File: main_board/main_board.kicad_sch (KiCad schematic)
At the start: 56 parts, among them J1 USB4105-GF-A-060, J2 Conn_ARM_JTAG_SWD_10, Q3 NX3008PBK,215, U1 SSD1306, U2 ESP32-S2-SOLO, U3 TLV62568PDRLT, U4 MCP73832, U5 DW01, U6 8205A, U7 MAX17055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

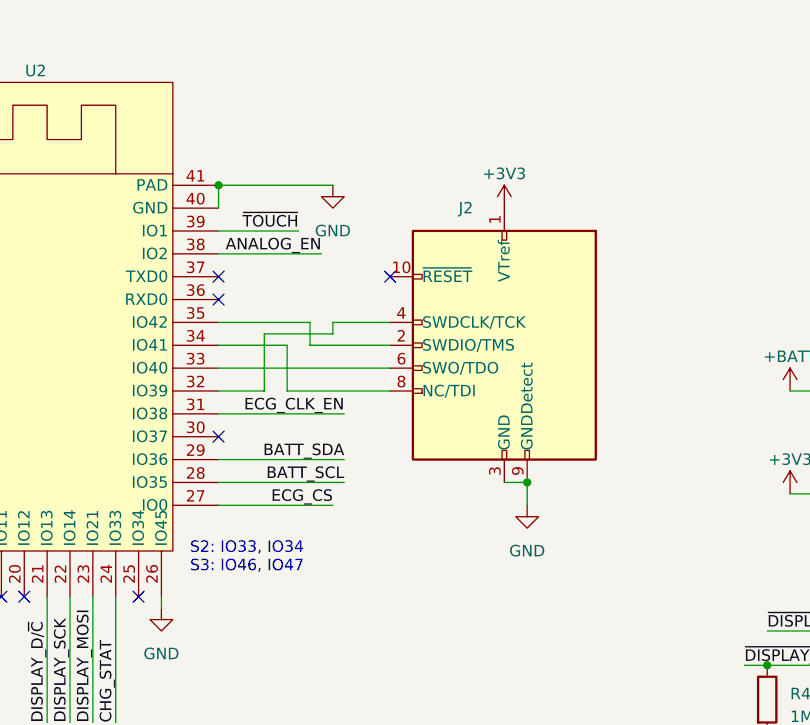
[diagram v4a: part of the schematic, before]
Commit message: Remove JTAG port
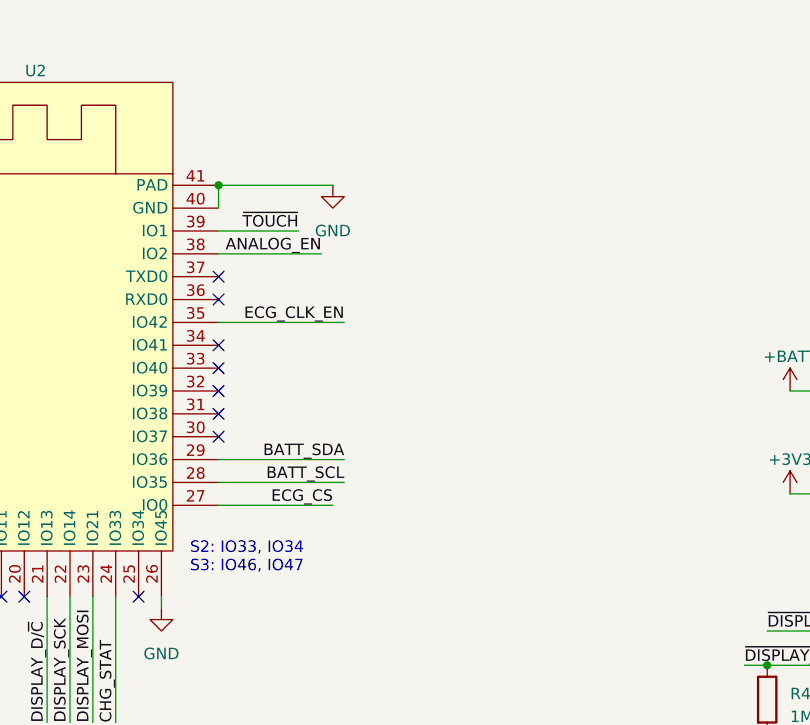
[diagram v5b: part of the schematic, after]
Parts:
- removed J2: Conn_ARM_JTAG_SWD_10, Connector:Tag-Connect_TC2050-IDC-NL_2x05_P1.27mm_Vertical, symbol Connector:Conn_ARM_JTAG_SWD_10
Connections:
- net ECG_CLK_EN: now also U2.35 (IO42); no longer U2.31 (IO38)
- no-connect marks 16 -> 19
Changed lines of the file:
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@@
   (junction (at 200.66 130.81) (diameter 0) (color 0 0 0 0)
   )
-  (junction (at 204.47 66.04) (diameter 0) (color 0 0 0 0)
-  )
   (junction (at 71.12 139.7) (diameter 0) (color 0 0 0 0)
   )
@@
   (junction (at 102.87 55.88) (diameter 0) (color 0 0 0 0)
   )
+  (no_connect (at 170.18 55.88))
+  (no_connect (at 170.18 53.34))
   (no_connect (at 254 109.22))
   (no_connect (at 138.43 78.74))
   (no_connect (at 170.18 60.96))
+  (no_connect (at 170.18 58.42))
   (no_connect (at 170.18 45.72))
-  (no_connect (at 189.23 43.18))
   (no_connect (at 198.12 144.78))
   (no_connect (at 148.59 78.74))
@@
   (no_connect (at 198.12 147.32))
   (no_connect (at 81.28 162.56))
+  (no_connect (at 170.18 50.8))
   (wire (pts (xy 116.84 58.42) (xy 129.54 58.42))
     (stroke (width 0) (type default))
@@
     (stroke (width 0) (type default))
   )
-  (wire (pts (xy 180.34 48.26) (xy 180.34 50.8))
-    (stroke (width 0) (type default))
-  )
   (wire (pts (xy 121.92 35.56) (xy 129.54 35.56))
     (stroke (width 0) (type default))
@@
     (stroke (width 0) (type default))
   )
-  (wire (pts (xy 177.8 50.8) (xy 177.8 55.88))
-    (stroke (width 0) (type default))
-  )
   (wire (pts (xy 158.75 177.8) (xy 158.75 186.69))
     (stroke (width 0) (type default))
@@
     (stroke (width 0) (type default))
   )
-  (wire (pts (xy 182.88 48.26) (xy 189.23 48.26))
-    (stroke (width 0) (type default))
-  )
   (wire (pts (xy 198.12 121.92) (xy 201.93 121.92))
     (stroke (width 0) (type default))
@@
     (stroke (width 0) (type default))
   )
-  (wire (pts (xy 182.88 49.53) (xy 182.88 48.26))
-    (stroke (width 0) (type default))
-  )
   (wire (pts (xy 129.54 175.26) (xy 129.54 177.8))
     (stroke (width 0) (type default))
@@
     (stroke (width 0) (type default))
   )
-  (wire (pts (xy 180.34 50.8) (xy 189.23 50.8))
-    (stroke (width 0) (type default))
-  )
   (wire (pts (xy 33.02 130.81) (xy 33.02 134.62))
     (stroke (width 0) (type default))
@@
     (stroke (width 0) (type default))
   )
-  (wire (pts (xy 175.26 55.88) (xy 175.26 49.53))
-    (stroke (width 0) (type default))
-  )
   (wire (pts (xy 80.01 134.62) (xy 82.55 134.62))
     (stroke (width 0) (type default))
   )
-  (wire (pts (xy 170.18 50.8) (xy 177.8 50.8))
-    (stroke (width 0) (type default))
-  )
   (wire (pts (xy 26.67 151.13) (xy 26.67 165.1))
     (stroke (width 0) (type default))
@@
     (stroke (width 0) (type default))
   )
-  (wire (pts (xy 170.18 48.26) (xy 180.34 48.26))
-    (stroke (width 0) (type default))
-  )
   (wire (pts (xy 240.03 52.07) (xy 254 52.07))
     (stroke (width 0) (type default))
@@
     (stroke (width 0) (type default))
   )
-  (wire (pts (xy 204.47 66.04) (xy 201.93 66.04))
-    (stroke (width 0) (type default))
-  )
   (wire (pts (xy 175.26 154.94) (xy 179.07 154.94))
     (stroke (width 0) (type default))
@@
     (stroke (width 0) (type default))
   )
-  (wire (pts (xy 204.47 68.58) (xy 204.47 66.04))
-    (stroke (width 0) (type default))
-  )
   (wire (pts (xy 238.76 67.31) (xy 254 67.31))
     (stroke (width 0) (type default))
@@
     (stroke (width 0) (type default))
   )
-  (wire (pts (xy 170.18 55.88) (xy 175.26 55.88))
-    (stroke (width 0) (type default))
-  )
   (wire (pts (xy 198.12 137.16) (xy 200.66 137.16))
     (stroke (width 0) (type default))
@@
     (stroke (width 0) (type default))
   )
-  (wire (pts (xy 170.18 58.42) (xy 184.15 58.42))
+  (wire (pts (xy 170.18 48.26) (xy 184.15 48.26))
     (stroke (width 0) (type default))
   )
@@
     (stroke (width 0) (type default))
   )
-  (wire (pts (xy 170.18 53.34) (xy 189.23 53.34))
-    (stroke (width 0) (type default))
-  )
   (wire (pts (xy 129.54 186.69) (xy 137.16 186.69))
     (stroke (width 0) (type default))
@@
     (stroke (width 0) (type default))
   )
-  (wire (pts (xy 177.8 55.88) (xy 189.23 55.88))
-    (stroke (width 0) (type default))
-  )
   (wire (pts (xy 248.92 128.27) (xy 254 128.27))
     (stroke (width 0) (type default))
@@
     (stroke (width 0) (type default))
   )
-  (wire (pts (xy 175.26 49.53) (xy 182.88 49.53))
-    (stroke (width 0) (type default))
-  )
   (wire (pts (xy 153.67 78.74) (xy 153.67 92.71))
     (stroke (width 0) (type default))
@@
     (effects (font (size 1.27 1.27)) (justify left bottom))
   )
-  (label "ECG_CLK_EN" (at 184.15 58.42 180) (fields_autoplaced)
+  (label "ECG_CLK_EN" (at 184.15 48.26 180) (fields_autoplaced)
     (effects (font (size 1.27 1.27)) (justify right bottom))
   )
@@
     )
   )
-  (symbol (lib_id "power:GND") (at 204.47 68.58 0) (mirror y) (unit 1)
-    (in_bom yes) (on_board yes) (dnp no) (fields_autoplaced)
-    (property "Reference" "#PWR012" (at 204.47 74.93 0)
-      (effects (font (size 1.27 1.27)) hide)
-    )
-    (property "Value" "GND" (at 204.47 73.66 0)
-      (effects (font (size 1.27 1.27)))
-    )
-    (property "Footprint" "" (at 204.47 68.58 0)
-      (effects (font (size 1.27 1.27)) hide)
-    )
-    (property "Datasheet" "" (at 204.47 68.58 0)
-      (effects (font (size 1.27 1.27)) hide)
-    )
-    (pin "1")
-    (instances
-      (project "main_board"
-        (path "/e55848cd-275a-4b5e-8e68-b5d8d07c8d31"
-          (reference "#PWR012") (unit 1)
-        )
-      )
-    )
-  )
   (symbol (lib_id "power:GND") (at 115.57 148.59 0) (unit 1)
     (in_bom yes) (on_board yes) (dnp no)
@@
     )
   )
-  (symbol (lib_id "power:+3V3") (at 201.93 35.56 0) (mirror y) (unit 1)
-    (in_bom yes) (on_board yes) (dnp no) (fields_autoplaced)
-    (property "Reference" "#PWR011" (at 201.93 39.37 0)
-      (effects (font (size 1.27 1.27)) hide)
-    )
-    (property "Value" "+3V3" (at 201.93 31.75 0)
-      (effects (font (size 1.27 1.27)))
-    )
-    (property "Footprint" "" (at 201.93 35.56 0)
-      (effects (font (size 1.27 1.27)) hide)
-    )
-    (property "Datasheet" "" (at 201.93 35.56 0)
-      (effects (font (size 1.27 1.27)) hide)
-    )
-    (pin "1")
-    (instances
-      (project "main_board"
-        (path "/e55848cd-275a-4b5e-8e68-b5d8d07c8d31"
-          (reference "#PWR011") (unit 1)
-        )
-      )
-    )
-  )
   (symbol (lib_id "main_board_parts:logo") (at 182.88 168.91 0) (unit 1)
     (in_bom no) (on_board yes) (dnp no)
@@
         )
       )
-    )
-  )
-  (symbol (lib_id "Connector:Conn_ARM_JTAG_SWD_10") (at 201.93 50.8 0) (mirror y) (unit 1)
-    (in_bom no) (on_board yes) (dnp no)
-    (property "Reference" "J2" (at 196.85 35.56 0)
-      (effects (font (size 1.27 1.27)) (justify right))
-    )
-    (property "Value" "Conn_ARM_JTAG_SWD_10" (at 190.5 67.31 0)
-      (effects (font (size 1.27 1.27)) (justify right) hide)
-    )
-    (property "Footprint" "Connector:Tag-Connect_TC2050-IDC-NL_2x05_P1.27mm_Vertical" (at 201.93 50.8 0)
-      (effects (font (size 1.27 1.27)) hide)
-    )
-    (property "Datasheet" "http://infocenter.arm.com/help/topic/com.arm.doc.ddi0314h/DDI0314H_coresight_components_trm.pdf" (at 210.82 82.55 90)
-      (effects (font (size 1.27 1.27)) hide)
-    )
-    (pin "1")
-    (pin "10")
-    (pin "2")
-    (pin "3")
-    (pin "4")
-    (pin "5")
-    (pin "6")
-    (pin "7")
-    (pin "8")
-    (pin "9")
-    (instances
-      (project "main_board"
-        (path "/e55848cd-275a-4b5e-8e68-b5d8d07c8d31"
-          (reference "J2") (unit 1)
-        )
-      )

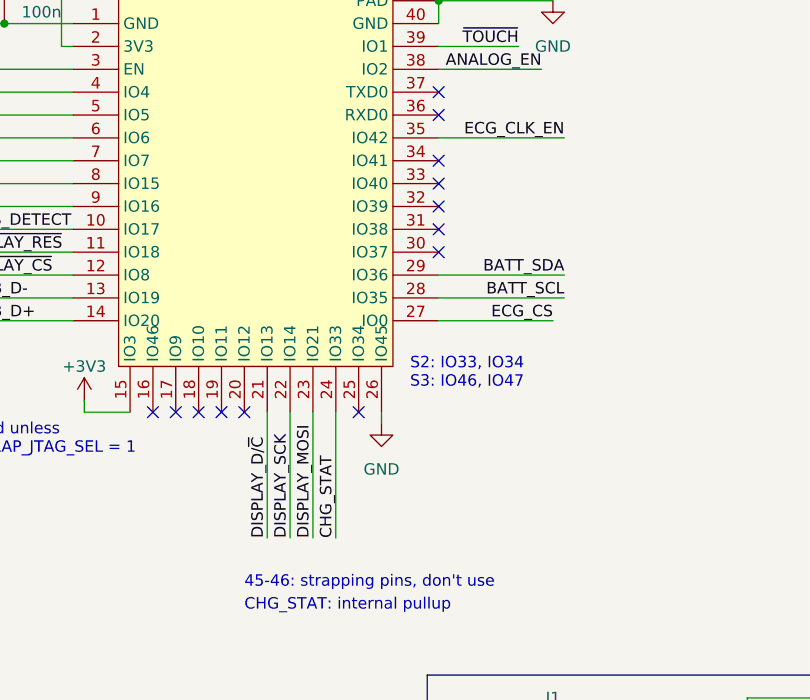
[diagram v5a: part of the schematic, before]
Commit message: Move display SPI to the right side of the module
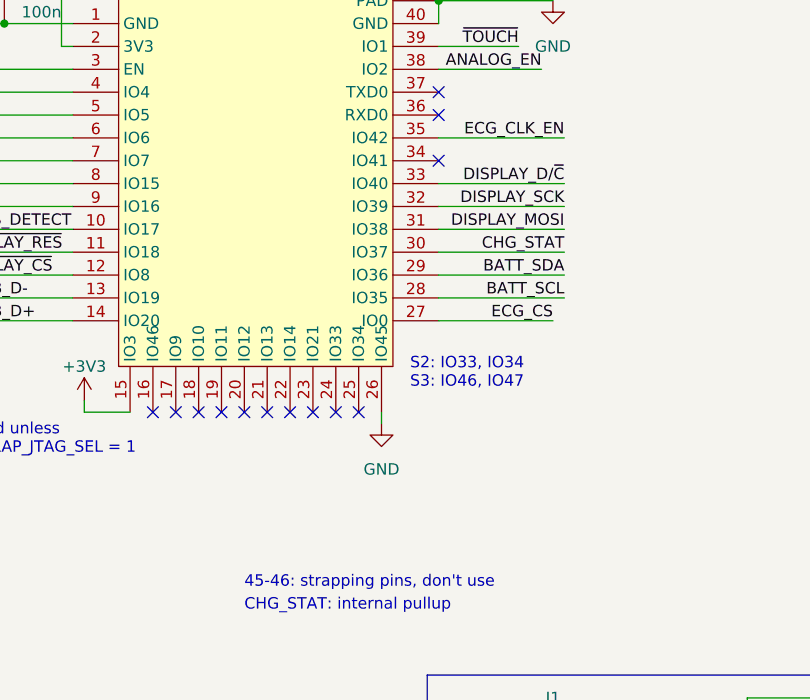
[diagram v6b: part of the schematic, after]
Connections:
- net CHG_STAT: now also U2.30 (IO37); no longer U2.24 (IO33)
- net DISPLAY_D/~{C}: now also U2.33 (IO40); no longer U2.21 (IO13)
- net DISPLAY_MOSI: now also U2.31 (IO38); no longer U2.23 (IO21)
- net DISPLAY_SCK: now also U2.32 (IO39); no longer U2.22 (IO14)
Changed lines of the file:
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@@
   (junction (at 102.87 55.88) (diameter 0) (color 0 0 0 0)
   )
-  (no_connect (at 170.18 55.88))
-  (no_connect (at 170.18 53.34))
+  (no_connect (at 158.75 78.74))
   (no_connect (at 254 109.22))
   (no_connect (at 138.43 78.74))
-  (no_connect (at 170.18 60.96))
-  (no_connect (at 170.18 58.42))
+  (no_connect (at 153.67 78.74))
   (no_connect (at 170.18 45.72))
   (no_connect (at 198.12 144.78))
@@
   (no_connect (at 81.28 162.56))
   (no_connect (at 170.18 50.8))
+  (no_connect (at 151.13 78.74))
+  (no_connect (at 156.21 78.74))
   (wire (pts (xy 116.84 58.42) (xy 129.54 58.42))
     (stroke (width 0) (type default))
@@
     (stroke (width 0) (type default))
   )
-  (wire (pts (xy 151.13 78.74) (xy 151.13 92.71))
+  (wire (pts (xy 170.18 53.34) (xy 184.15 53.34))
     (stroke (width 0) (type default))
   )
@@
     (stroke (width 0) (type default))
   )
-  (wire (pts (xy 156.21 78.74) (xy 156.21 92.71))
+  (wire (pts (xy 170.18 58.42) (xy 184.15 58.42))
     (stroke (width 0) (type default))
   )
@@
     (stroke (width 0) (type default))
   )
-  (wire (pts (xy 158.75 92.71) (xy 158.75 78.74))
+  (wire (pts (xy 184.15 60.96) (xy 170.18 60.96))
     (stroke (width 0) (type default))
   )
@@
     (stroke (width 0) (type default))
   )
-  (wire (pts (xy 153.67 78.74) (xy 153.67 92.71))
+  (wire (pts (xy 170.18 55.88) (xy 184.15 55.88))
     (stroke (width 0) (type default))
   )
@@
     (effects (font (size 1.27 1.27)) (justify right bottom))
   )
-  (label "DISPLAY_SCK" (at 153.67 92.71 90) (fields_autoplaced)
-    (effects (font (size 1.27 1.27)) (justify left bottom))
+  (label "DISPLAY_SCK" (at 184.15 55.88 180) (fields_autoplaced)
+    (effects (font (size 1.27 1.27)) (justify right bottom))
   )
   (label "USB_D+" (at 118.11 68.58 0) (fields_autoplaced)
@@
     (effects (font (size 1.27 1.27)) (justify left bottom))
   )
-  (label "CHG_STAT" (at 158.75 92.71 90) (fields_autoplaced)
-    (effects (font (size 1.27 1.27)) (justify left bottom))
+  (label "CHG_STAT" (at 184.15 60.96 180) (fields_autoplaced)
+    (effects (font (size 1.27 1.27)) (justify right bottom))
   )
   (label "USB_D-" (at 118.11 66.04 0) (fields_autoplaced)
@@
     (effects (font (size 1.27 1.27)) (justify right bottom))
   )
-  (label "DISPLAY_D{slash}~{C}" (at 151.13 92.71 90) (fields_autoplaced)
-    (effects (font (size 1.27 1.27)) (justify left bottom))
+  (label "DISPLAY_D{slash}~{C}" (at 184.15 53.34 180) (fields_autoplaced)
+    (effects (font (size 1.27 1.27)) (justify right bottom))
   )
   (label "USB_D+" (at 208.28 135.89 180) (fields_autoplaced)
@@
     (effects (font (size 1.27 1.27)) (justify left bottom))
   )
-  (label "DISPLAY_MOSI" (at 156.21 92.71 90) (fields_autoplaced)
-    (effects (font (size 1.27 1.27)) (justify left bottom))
+  (label "DISPLAY_MOSI" (at 184.15 58.42 180) (fields_autoplaced)
+    (effects (font (size 1.27 1.27)) (justify right bottom))
   )
   (label "ANALOG_EN" (at 43.18 182.88 180) (fields_autoplaced)

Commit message: Clean up
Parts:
- added J2: Conn_01x06_Pin, Connector_Molex:Molex_Pico-Clasp_501331-0607_1x06-1MP_P1.00mm_Vertical, symbol Connector_Generic_MountingPin:Conn_01x06_MountingPin
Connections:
- net +3V3: now also J2.5 (Pin_5)
- net ECG_CS: now also J2.1 (Pin_1)
- net EN: now also J2.6 (Pin_6)
- net GND: now also J2.3 (Pin_3), J2.MP (MountPin)
- net at U2.36 (RXD0): now also J2.2 (Pin_2)
- net at U2.37 (TXD0): now also J2.4 (Pin_4)
- no-connect marks 19 -> 17
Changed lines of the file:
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@@
   (no_connect (at 138.43 78.74))
   (no_connect (at 153.67 78.74))
-  (no_connect (at 170.18 45.72))
   (no_connect (at 198.12 144.78))
   (no_connect (at 148.59 78.74))
-  (no_connect (at 170.18 43.18))
   (no_connect (at 139.7 170.18))
   (no_connect (at 143.51 78.74))
@@
     (stroke (width 0) (type default))
   )
+  (wire (pts (xy 195.58 50.8) (xy 205.74 50.8))
+    (stroke (width 0) (type default))
+  )
   (wire (pts (xy 200.66 134.62) (xy 200.66 135.89))
     (stroke (width 0) (type default))
@@
     (stroke (width 0) (type default))
   )
+  (wire (pts (xy 195.58 68.58) (xy 195.58 50.8))
+    (stroke (width 0) (type default))
+  )
   (wire (pts (xy 74.93 120.65) (xy 74.93 121.92))
     (stroke (width 0) (type default))
@@
     (stroke (width 0) (type default))
   )
+  (wire (pts (xy 200.66 45.72) (xy 200.66 55.88))
+    (stroke (width 0) (type default))
+  )
   (wire (pts (xy 198.12 121.92) (xy 201.93 121.92))
     (stroke (width 0) (type default))
@@
     (stroke (width 0) (type default))
   )
+  (wire (pts (xy 200.66 38.1) (xy 205.74 38.1))
+    (stroke (width 0) (type default))
+  )
   (wire (pts (xy 137.16 177.8) (xy 137.16 180.34))
     (stroke (width 0) (type default))
@@
     (stroke (width 0) (type default))
   )
+  (wire (pts (xy 210.82 33.02) (xy 215.9 33.02))
+    (stroke (width 0) (type default))
+  )
   (wire (pts (xy 238.76 90.17) (xy 254 90.17))
     (stroke (width 0) (type default))
@@
     (stroke (width 0) (type default))
   )
+  (wire (pts (xy 195.58 40.64) (xy 205.74 40.64))
+    (stroke (width 0) (type default))
+  )
   (wire (pts (xy 254 71.12) (xy 246.38 71.12))
     (stroke (width 0) (type default))
@@
     (stroke (width 0) (type default))
   )
+  (wire (pts (xy 170.18 45.72) (xy 195.58 45.72))
+    (stroke (width 0) (type default))
+  )
   (wire (pts (xy 73.66 165.1) (xy 74.93 165.1))
     (stroke (width 0) (type default))
@@
     (stroke (width 0) (type default))
   )
+  (wire (pts (xy 195.58 48.26) (xy 205.74 48.26))
+    (stroke (width 0) (type default))
+  )
   (wire (pts (xy 139.7 175.26) (xy 129.54 175.26))
     (stroke (width 0) (type default))
@@
     (stroke (width 0) (type default))
   )
+  (wire (pts (xy 170.18 43.18) (xy 205.74 43.18))
+    (stroke (width 0) (type default))
+  )
   (wire (pts (xy 247.65 48.26) (xy 254 48.26))
     (stroke (width 0) (type default))
@@
     (stroke (width 0) (type default))
   )
+  (wire (pts (xy 195.58 45.72) (xy 195.58 48.26))
+    (stroke (width 0) (type default))
+  )
   (wire (pts (xy 120.65 138.43) (xy 120.65 139.7))
     (stroke (width 0) (type default))
@@
     (stroke (width 0) (type default))
   )
-  (wire (pts (xy 170.18 68.58) (xy 182.88 68.58))
+  (wire (pts (xy 170.18 68.58) (xy 195.58 68.58))
     (stroke (width 0) (type default))
   )
@@
   )
   (wire (pts (xy 69.85 45.72) (xy 129.54 45.72))
+    (stroke (width 0) (type default))
+  )
+  (wire (pts (xy 205.74 45.72) (xy 200.66 45.72))
     (stroke (width 0) (type default))
   )
@@
   (label "BATT_SCL" (at 165.1 172.72 180) (fields_autoplaced)
     (effects (font (size 1.27 1.27)) (justify right bottom))
+  )
+  (label "EN" (at 200.66 38.1 0) (fields_autoplaced)
+    (effects (font (size 1.27 1.27)) (justify left bottom))
   )
   (label "BATT_SDA" (at 25.4 194.31 0) (fields_autoplaced)
@@
     )
   )
+  (symbol (lib_id "power:GND") (at 200.66 55.88 0) (mirror y) (unit 1)
+    (in_bom yes) (on_board yes) (dnp no)
+    (property "Reference" "#PWR012" (at 200.66 62.23 0)
+      (effects (font (size 1.27 1.27)) hide)
+    )
+    (property "Value" "GND" (at 200.66 60.96 0)
+      (effects (font (size 1.27 1.27)))
+    )
+    (property "Footprint" "" (at 200.66 55.88 0)
+      (effects (font (size 1.27 1.27)) hide)
+    )
+    (property "Datasheet" "" (at 200.66 55.88 0)
+      (effects (font (size 1.27 1.27)) hide)
+    )
+    (pin "1")
+    (instances
+      (project "main_board"
+        (path "/e55848cd-275a-4b5e-8e68-b5d8d07c8d31"
+          (reference "#PWR012") (unit 1)
+        )
+      )
+    )
+  )
   (symbol (lib_id "Device:R") (at 148.59 186.69 270) (unit 1)
     (in_bom yes) (on_board yes) (dnp no)
@@
     )
   )
+  (symbol (lib_id "power:GND") (at 215.9 33.02 0) (mirror y) (unit 1)
+    (in_bom yes) (on_board yes) (dnp no)
+    (property "Reference" "#PWR013" (at 215.9 39.37 0)
+      (effects (font (size 1.27 1.27)) hide)
+    )
+    (property "Value" "GND" (at 215.9 38.1 0)
+      (effects (font (size 1.27 1.27)))
+    )
+    (property "Footprint" "" (at 215.9 33.02 0)
+      (effects (font (size 1.27 1.27)) hide)
+    )
+    (property "Datasheet" "" (at 215.9 33.02 0)
+      (effects (font (size 1.27 1.27)) hide)
+    )
+    (pin "1")
+    (instances
+      (project "main_board"
+        (path "/e55848cd-275a-4b5e-8e68-b5d8d07c8d31"
+          (reference "#PWR013") (unit 1)
+        )
+      )
+    )
+  )
   (symbol (lib_id "Device:C") (at 243.84 40.64 90) (unit 1)
     (in_bom yes) (on_board yes) (dnp no)
@@
         (path "/e55848cd-275a-4b5e-8e68-b5d8d07c8d31"
           (reference "C13") (unit 1)
+        )
+      )
+    )
+  )
+  (symbol (lib_id "Connector_Generic_MountingPin:Conn_01x06_MountingPin") (at 210.82 45.72 0) (mirror x) (unit 1)
+    (in_bom yes) (on_board yes) (dnp no)
+    (property "Reference" "J2" (at 214.63 45.72 0)
+      (effects (font (size 1.27 1.27)) (justify right))
+    )
+    (property "Value" "Conn_01x06_Pin" (at 222.25 54.61 0)
+      (effects (font (size 1.27 1.27)) (justify right))
+    )
+    (property "Footprint" "Connector_Molex:Molex_Pico-Clasp_501331-0607_1x06-1MP_P1.00mm_Vertical" (at 210.82 45.72 0)
+      (effects (font (size 1.27 1.27)) hide)
+    )
+    (property "Datasheet" "~" (at 210.82 45.72 0)
+      (effects (font (size 1.27 1.27)) hide)
+    )
+    (pin "1")
+    (pin "2")
+    (pin "3")
+    (pin "4")
+    (pin "5")
+    (pin "6")
+    (pin "MP")
+    (instances
+      (project "main_board"
+        (path "/e55848cd-275a-4b5e-8e68-b5d8d07c8d31"
+          (reference "J2") (unit 1)
         )
       )
@@
         )
       )
+    )
+  )
+  (symbol (lib_id "power:+3V3") (at 195.58 40.64 0) (unit 1)
+    (in_bom yes) (on_board yes) (dnp no)
+    (property "Reference" "#PWR011" (at 195.58 44.45 0)
+      (effects (font (size 1.27 1.27)) hide)
+    )
+    (property "Value" "+3V3" (at 198.755 39.37 0)
+      (effects (font (size 1.27 1.27)))
+    )
+    (property "Footprint" "" (at 195.58 40.64 0)
+      (effects (font (size 1.27 1.27)) hide)
+    )
+    (property "Datasheet" "" (at 195.58 40.64 0)
+      (effects (font (size 1.27 1.27)) hide)
+    )
+    (pin "1")
+    (instances
+      (project "main_board"
+        (path "/e55848cd-275a-4b5e-8e68-b5d8d07c8d31"
+          (reference "#PWR011") (unit 1)
+        )
+      )
